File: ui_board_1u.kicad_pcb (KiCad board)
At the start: 2 copper layers, 156 x 38 mm, 114 parts, among them J2 X9555WV-2x06-6TV01, SW1 PEC164220F-S0024, SW2 B3FS-1052, SW3 291V1022F832AB, SW4 MS-22C01-G010, U1 SSD1322, U2 MCP23S17_ML, U4 TPS61040DBV, U6 SPX3819M5-L

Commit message: add QR code to silkscreen, add render images
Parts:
- removed the G*** at (189.0, 67.0)
- added G***: LOGO, LOGO, B.Cu at (129.8, 88.5)
- added G***: LOGO, LOGO, B.Cu at (118.5, 85.8)
- added kibuzzard-693EBA51: G***, kibuzzard-693EBA51, B.Cu at (155.0, 67.8)
- moved REF** 34.8 mm to (137.5, 89.0)
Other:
- board text added: "Rev: - 12/2025"
- board text added: "https://github.com/ betz-engineering/ ui_board_1u"
- board text removed: "Rev: -"
- board text removed: "ui_board_1u"

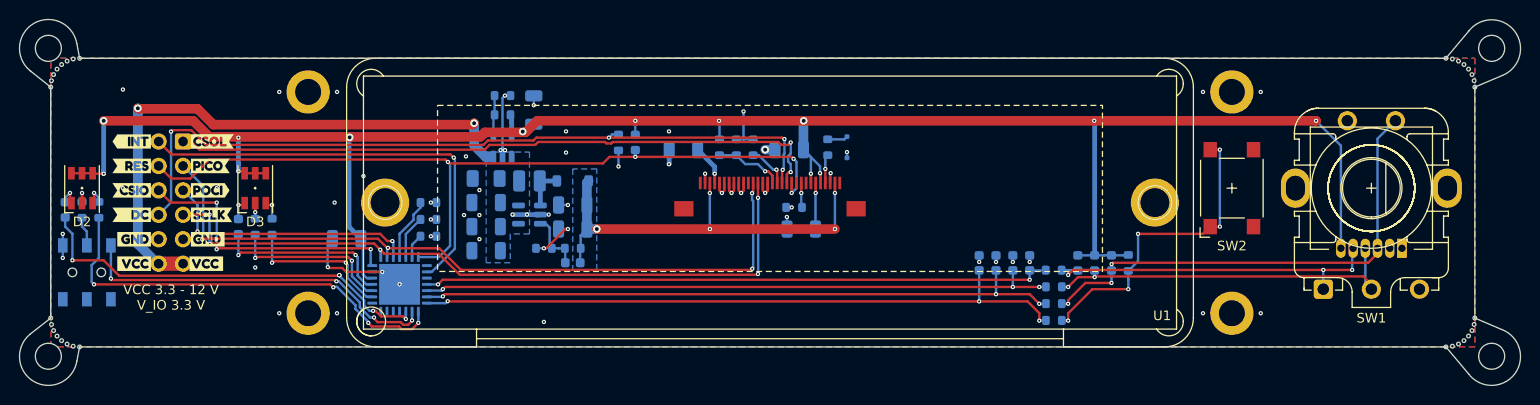
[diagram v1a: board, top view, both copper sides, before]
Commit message: optimize component values for easier production
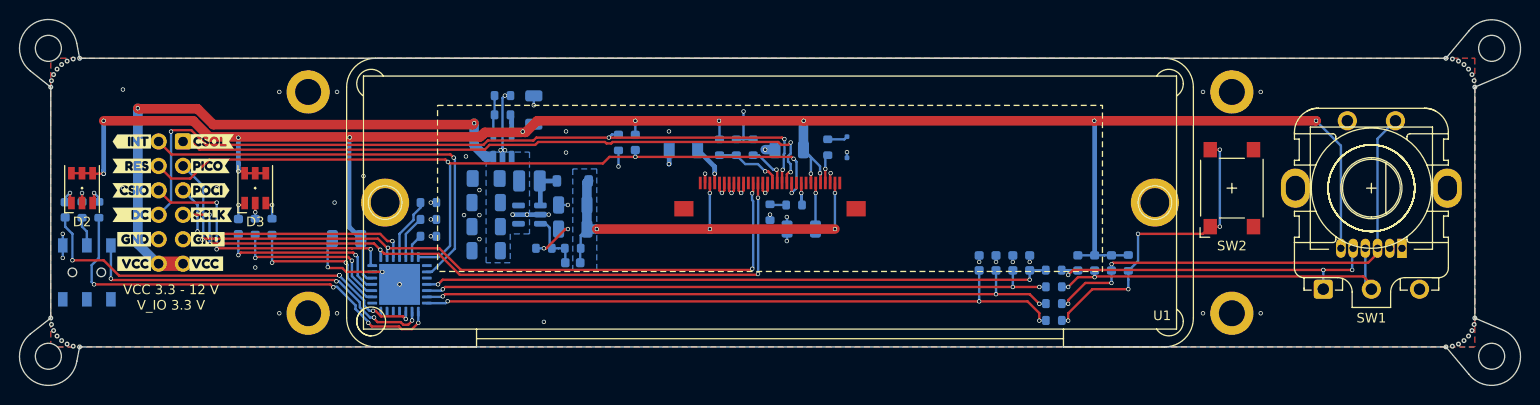
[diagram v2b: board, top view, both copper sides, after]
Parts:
- removed REF**: OSHW-Logo2_7.3x6mm_SilkScreen, Symbol:OSHW-Logo2_7.3x6mm_SilkScreen
- added R27: 470k, Resistor_SMD:R_0603_1608Metric, B.Cu at (128.0, 78.8)
- C8: value 4p7 -> 10p
- R10, R8: value 160R -> 560R
- R11, R9: value 160R -> 150R
- R20: value 680k -> 200k
- R23: value 50R -> 51R
- R24: value 1M8 -> 330k
- R25: value 205k -> 33k
- R42: value 37k4 -> 51k
- R45: value 22k -> 30k
- R5, R6: value 160R -> 22R
- SW2: value B3FS-1052 -> ZX-QC66-7.5TP
- U1: value SSD1322 -> AFC01-S30FCA-00
- moved R20 2.55 mm to (125.5, 79.5), turned to -90 degrees
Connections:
- R20 pad 1: Net-(U1-IREF) -> Net-(R20-Pad1)
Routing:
- net Net-(R20-Pad1): track 0.00 -> 1.71 mm
- net Net-(U1-IREF): track 2.57 -> 3.85 mm
- net GND: track 61.1 -> 62.3 mm, vias 58 -> 59

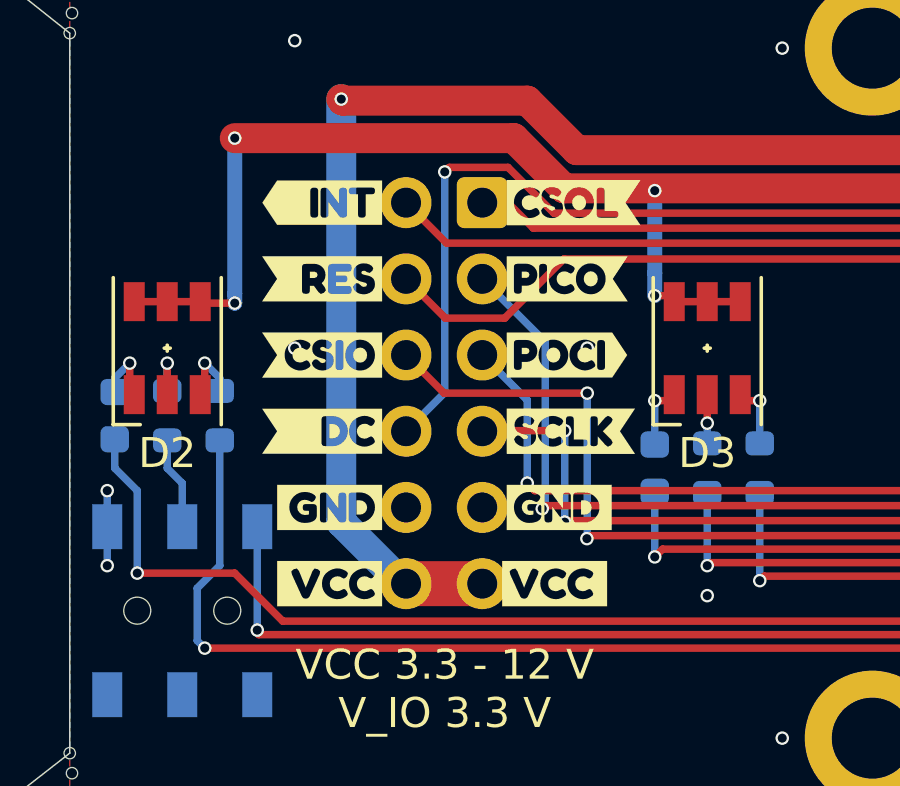
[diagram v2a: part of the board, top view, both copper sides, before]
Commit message: rename POCI and PICO signals to SDO and SDI
according to the OSHWA recommendation
https://oshwa.org/resources/a-resolution-to-redefine-spi-signal-names/
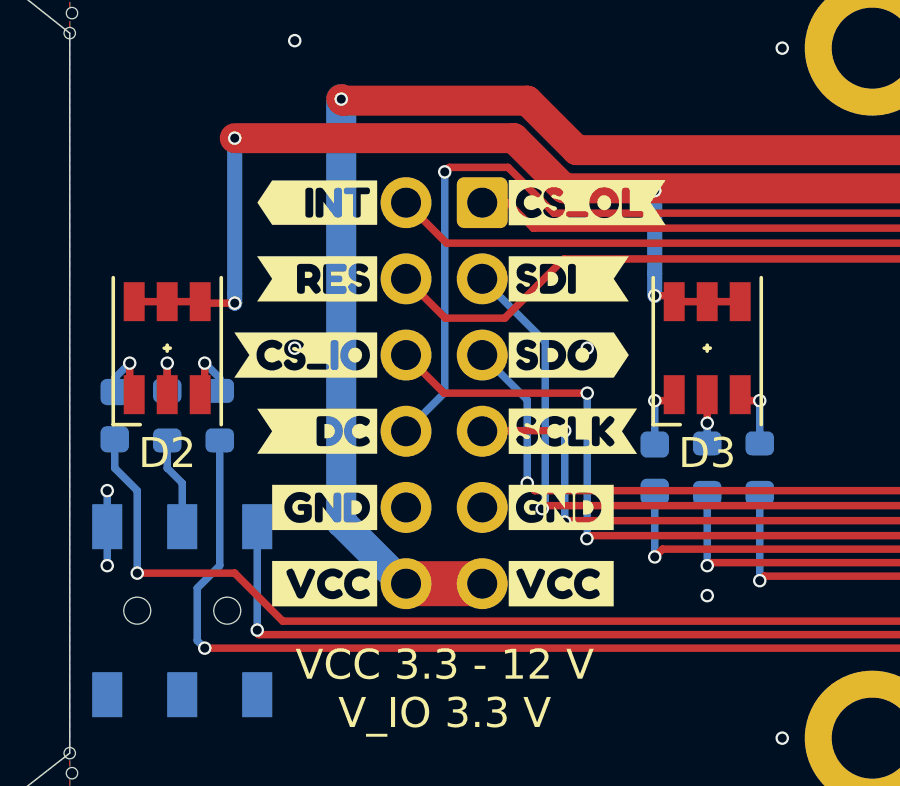
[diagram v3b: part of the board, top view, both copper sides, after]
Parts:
- removed kibuzzard-693D4BF5: G***, kibuzzard-693D4BF5
- removed kibuzzard-693D4BFC: G***, kibuzzard-693D4BFC
- removed kibuzzard-693D4C0F: G***, kibuzzard-693D4C0F
- removed kibuzzard-693D4C3C: G***, kibuzzard-693D4C3C
- added kibuzzard-69405870: G***, kibuzzard-69405870, F.Cu at (67.4, 74.7)
- added kibuzzard-6940587B: G***, kibuzzard-6940587B, F.Cu at (67.4, 77.3)
- added kibuzzard-69405890: G***, kibuzzard-69405890, F.Cu at (58.6, 77.3)
- added kibuzzard-6940589C: G***, kibuzzard-6940589C, F.Cu at (68.0, 72.2)
- moved kibuzzard-693D4BDF 0.22 mm to (67.1, 84.9)
- moved kibuzzard-693D4C36 0.17 mm to (59.0, 74.7)
- moved kibuzzard-693D4C42 0.17 mm to (59.0, 79.8)
- moved kibuzzard-693D4C48 0.17 mm to (59.3, 82.3)
- moved kibuzzard-693D4C4F 0.17 mm to (59.3, 84.9)
- moved kibuzzard-693D4C30 0.17 mm to (59.0, 72.2)
- moved kibuzzard-693D4BE6 0.07 mm to (67.1, 82.3)
- moved kibuzzard-693D4BEE 0.07 mm to (67.5, 79.8)
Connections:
- net PICO renamed SDI
- net POCI renamed SDO

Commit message: fix / ignore all remaining DRC errors
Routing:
- net GND: track 62.3 -> 62.2 mm, vias 59 -> 58
- net /Switches and LEDs/LEDA_B: vias 5 -> 4

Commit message: geographical re-annotate
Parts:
- renumbered C15 to C1, C4 to C10, C5 to C11, C6 to C12, C7 to C13, C13 to C14, C8 to C15, C12 to C2, C10 to C3, C2 to C4, C9 to C5, C1 to C6, C11 to C7, C14 to C8, C17 to C9, D2 to D1, D3 to D2, D1 to D3, D5 to D4, G*** to G?, H5 to H1, H14 to H10, H13 to H11, H6 to H12, H10 to H13, H11 to H14, H12 to H15, H1 to H16, H2 to H17, H15 to H18, H16 to H19, H13 to H2, H17 to H20, H3 to H21, H4 to H22, H14 to H23, H16 to H24, H15 to H25, H17 to H26, H13 to H27, H11 to H28, H10 to H29, H14 to H3, H12 to H30, H13 to H31, H7 to H32, H12 to H33, H11 to H34, H10 to H35, H16 to H36, H17 to H37, H15 to H38, H14 to H39, H15 to H4, H8 to H40, H16 to H5, H17 to H6, H11 to H7, H10 to H8, H12 to H9, J2 to J1, R42 to R1, R20 to R10, R17 to R11, R9 to R12, R8 to R13, R5 to R14, R11 to R17, R10 to R18, R6 to R19, R45 to R2, R4 to R20, R3 to R21, R2 to R22, R1 to R23, R13 to R26, R12 to R27, R14 to R28, R26 to R29, R7 to R3, R22 to R4, R23 to R5, R19 to R6, R18 to R7, R21 to R8, R27 to R9, SW2 to SW1, SW3 to SW2, SW1 to SW3, U6 to U2, U4 to U3, U2 to U4, kibuzzard-693D4C30 to kibuzzard-1, kibuzzard-693D4BE6 to kibuzzard-10, kibuzzard-693D4C4F to kibuzzard-11, kibuzzard-693D4BDF to kibuzzard-12, kibuzzard-693D4AF8 to kibuzzard-13, kibuzzard-693EBA51 to kibuzzard-14, kibuzzard-693D4DAF to kibuzzard-15, kibuzzard-6940589C to kibuzzard-2, kibuzzard-693D4C36 to kibuzzard-3, kibuzzard-69405870 to kibuzzard-4, kibuzzard-69405890 to kibuzzard-5, kibuzzard-6940587B to kibuzzard-6, kibuzzard-693D4C42 to kibuzzard-7, kibuzzard-693D4BEE to kibuzzard-8, kibuzzard-693D4C48 to kibuzzard-9

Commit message: update schematic .pdf and pictures
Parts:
- added G2: OSHW-Logo2_9.8x8mm_SilkScreen, Symbol:OSHW-Logo2_9.8x8mm_SilkScreen, B.Cu at (138.0, 89.0)
- gave numbers to parts that had none: 2

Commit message: review OLED pinout, add 2 GND pins
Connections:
- U1 pad 1: unconnected-(U1-NC-Pad1) -> GND
- U1 pad 30: unconnected-(U1-NC-Pad30) -> GND

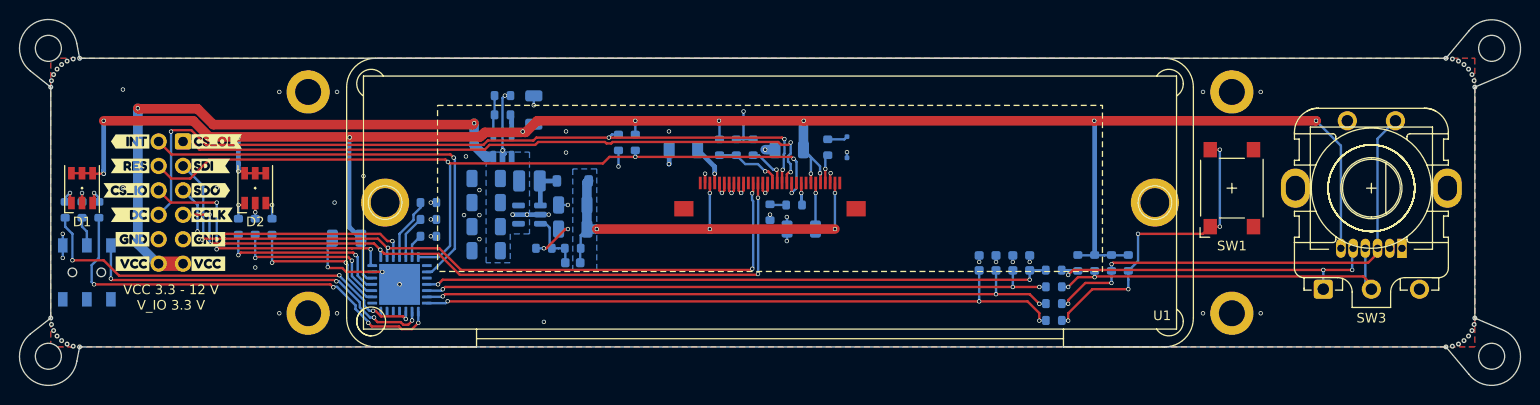
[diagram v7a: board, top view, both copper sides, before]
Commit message: add extension board connector
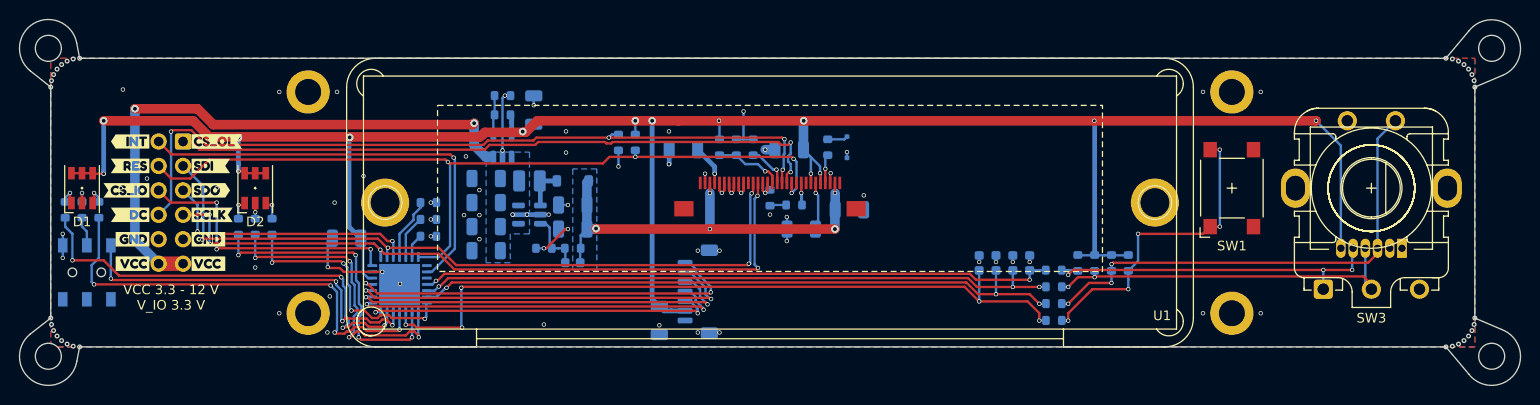
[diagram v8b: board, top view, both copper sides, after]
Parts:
- added C17: 4u7, Capacitor_SMD:C_1206_3216Metric, B.Cu at (114.0, 90.8)
- added C18: 4u7, Capacitor_SMD:C_1206_3216Metric, B.Cu at (133.8, 79.3)
- added J5: BM07B-SRSS-TB, Connector_JST:JST_SH_BM07B-SRSS-TB_1x07-1MP_P1.00mm_Vertical, B.Cu at (118.0, 87.8)
- added kibuzzard-694336A4: G***, kibuzzard-694336A4, B.Cu at (118.0, 81.3)
- moved G0 39.5 mm to (155.3, 71.3)
- moved G2 34.7 mm to (167.5, 70.7)
- moved kibuzzard-14 28.3 mm to (137.5, 90.0)
- moved G1 24.2 mm to (144.8, 69.5)
- moved R10 1.50 mm to (125.5, 78.0), turned to 90 degrees
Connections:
- SW4 pad 1: Net-(U4-GPA6) -> Net-(U4-GPB1)
- U4 pad 1: unconnected-(U4-GPB4-Pad1) -> /Switches and LEDs/GPB4
- U4 pad 2: /Switches and LEDs/LEDB_R -> /Switches and LEDs/GPB5
- U4 pad 21: /Switches and LEDs/BACK_SW -> /Switches and LEDs/LEDB_R
- U4 pad 22: /Switches and LEDs/LEDA_R -> /Switches and LEDs/LEDB_G
- U4 pad 23: Net-(U4-GPA6) -> /Switches and LEDs/LEDB_B
- U4 pad 24: /Switches and LEDs/LEDA_B -> /Switches and LEDs/BACK_SW
- U4 pad 25: unconnected-(U4-GPB0-Pad25) -> /Switches and LEDs/LEDA_R
- U4 pad 26: unconnected-(U4-GPB1-Pad26) -> Net-(U4-GPB1)
- U4 pad 27: unconnected-(U4-GPB2-Pad27) -> /Switches and LEDs/LEDA_B
- U4 pad 28: unconnected-(U4-GPB3-Pad28) -> /Switches and LEDs/GPB3
- U4 pad 3: /Switches and LEDs/LEDB_G -> /Switches and LEDs/GPB6
- U4 pad 4: /Switches and LEDs/LEDB_B -> /Switches and LEDs/GPB7
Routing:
- net /Switches and LEDs/GPB7: track 0.00 -> 41.5 mm, vias 0 -> 2
- net /Switches and LEDs/GPB6: track 0.00 -> 41.2 mm, vias 0 -> 2
- net /Switches and LEDs/GPB5: track 0.00 -> 40.2 mm, vias 0 -> 2
- net /Switches and LEDs/GPB4: track 0.00 -> 38.9 mm, vias 0 -> 2
- net Net-(U4-GPB1): track 0.00 -> 38.7 mm, vias 0 -> 4
- net Net-(U4-GPA6): track 38.3 -> 0.00 mm, vias 4 -> 0
- net /Switches and LEDs/GPB3: track 0.00 -> 36.3 mm, vias 0 -> 2
- net +3V3: track 211.6 -> 234.0 mm, vias 13 -> 14
- net /Switches and LEDs/LEDB_G: track 17.0 -> 31.9 mm, vias 2 -> 4
- net /Switches and LEDs/LEDB_B: track 18.7 -> 31.9 mm, vias 2 -> 4
- net /Switches and LEDs/LEDB_R: track 15.8 -> 25.7 mm, vias 2 -> 4
- net /Switches and LEDs/BACK_SW: track 68.9 -> 77.5 mm, vias 3 -> 5
- net /Switches and LEDs/LEDA_B: track 43.1 -> 45.7 mm
- net /Switches and LEDs/LEDA_R: track 44.7 -> 46.4 mm
- net GND: track 62.2 -> 60.7 mm, vias 58 -> 66
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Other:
- board text added: "3V3"
- board text added: "B3"
- board text added: "B4"
- board text added: "B5"
- board text added: "B6"
- board text added: "B7"
- board text added: "GND"
